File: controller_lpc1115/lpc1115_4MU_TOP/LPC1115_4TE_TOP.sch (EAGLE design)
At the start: 102 parts, among them P2 ISP, Q1 BC856, Q2 BCP52, Q3 BC847C, U1 LPC1115FBD48, U2 BD9G101, U3 XO32 12MHz

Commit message: [ctrl_4MU_TOP] - v2.0 alpha
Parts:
- added C25: 100nF, rcl:C-EUC1206
- C2: value 470n -> 470nF
- C20, C6: device rcl:C-EUC1206 -> rcl:C-EUC0805
- renumbered D9 to D100
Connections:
- net +3V3: now also C25.1
- net GND: now also C25.2
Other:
- moved on the sheet: C7
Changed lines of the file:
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@@
 <part name="L1" library="rcl" library_urn="urn:adsk.eagle:library:334" deviceset="L-EU" device="L4532P" package3d_urn="urn:adsk.eagle:package:23484/1" value="4.7uH"/>
 <part name="C4" library="rcl" library_urn="urn:adsk.eagle:library:334" deviceset="C-EU" device="C0805" package3d_urn="urn:adsk.eagle:package:23617/2" value="4.7uF 50V"/>
-<part name="C6" library="rcl" library_urn="urn:adsk.eagle:library:334" deviceset="C-EU" device="C1206" package3d_urn="urn:adsk.eagle:package:23618/2" value="47uF 10V"/>
+<part name="C6" library="rcl" library_urn="urn:adsk.eagle:library:334" deviceset="C-EU" device="C0805" package3d_urn="urn:adsk.eagle:package:23617/2" value="47uF 10V"/>
 <part name="C1" library="rcl" library_urn="urn:adsk.eagle:library:334" deviceset="C-EU" device="C0805" package3d_urn="urn:adsk.eagle:package:23617/2" value="15nF"/>
 <part name="R2" library="rcl" library_urn="urn:adsk.eagle:library:334" deviceset="R-EU_" device="R0805" package3d_urn="urn:adsk.eagle:package:23553/2" value="1k6"/>
 <part name="R5" library="rcl" library_urn="urn:adsk.eagle:library:334" deviceset="R-EU_" device="R0805" package3d_urn="urn:adsk.eagle:package:23553/2" value="470R"/>
-<part name="C2" library="rcl" library_urn="urn:adsk.eagle:library:334" deviceset="C-EU" device="C0805" package3d_urn="urn:adsk.eagle:package:23617/2" value="470n"/>
-<part name="D9" library="diode" deviceset="DIODE-" device="SOD123" value="RB060M-60(*)"/>
+<part name="C2" library="rcl" library_urn="urn:adsk.eagle:library:334" deviceset="C-EU" device="C0805" package3d_urn="urn:adsk.eagle:package:23617/2" value="470nF"/>
+<part name="D100" library="diode" deviceset="DIODE-" device="SOD123" value="RB060M-60(*)"/>
 <part name="+3V35" library="supply1" deviceset="+3V3" device=""/>
 <part name="C13" library="rcl" library_urn="urn:adsk.eagle:library:334" deviceset="C-EU" device="C0805" package3d_urn="urn:adsk.eagle:package:23617/2" value="1uF"/>
@@
 <part name="D15" library="Diode_for_Selfbus-Projects" deviceset="DIODE-ZENER" device="SOD-123" package3d_urn="urn:adsk.eagle:package:40015434/2" value="DDZ9685"/>
 <part name="R1" library="rcl" library_urn="urn:adsk.eagle:library:334" deviceset="R-EU_" device="R2512" package3d_urn="urn:adsk.eagle:package:23545/2" value="24R  2512 1.0W"/>
-<part name="C20" library="rcl" library_urn="urn:adsk.eagle:library:334" deviceset="C-EU" device="C1206" package3d_urn="urn:adsk.eagle:package:23618/2" value="47uF 10V"/>
+<part name="C20" library="rcl" library_urn="urn:adsk.eagle:library:334" deviceset="C-EU" device="C0805" package3d_urn="urn:adsk.eagle:package:23617/2" value="47uF 10V"/>
 <part name="GND4" library="supply1" deviceset="GND" device=""/>
 <part name="C21" library="rcl" library_urn="urn:adsk.eagle:library:334" deviceset="C-EU" device="C0805" package3d_urn="urn:adsk.eagle:package:23617/2" value="100nF"/>
 <part name="C8" library="rcl" library_urn="urn:adsk.eagle:library:334" deviceset="C-EU" device="C0805" package3d_urn="urn:adsk.eagle:package:23617/2" value="100nF"/>
 <part name="C24" library="rcl" library_urn="urn:adsk.eagle:library:334" deviceset="C-EU" device="C0805" package3d_urn="urn:adsk.eagle:package:23617/2" value="1uF"/>
+<part name="C25" library="rcl" library_urn="urn:adsk.eagle:library:334" deviceset="C-EU" device="C1206" package3d_urn="urn:adsk.eagle:package:23618/2" value="100nF"/>
+<part name="GND7" library="supply1" deviceset="GND" device=""/>
 </parts>
 <sheets>
@@
 <instance part="C6" gate="G$1" x="200.66" y="226.06" smashed="yes">
 <attribute name="NAME" x="202.184" y="226.441" size="1.778" layer="95"/>
-<attribute name="VALUE" x="206.629" y="211.074" size="1.778" layer="96" rot="R90"/>
+<attribute name="VALUE" x="201.549" y="190.754" size="1.778" layer="96" rot="R90"/>
 </instance>
 <instance part="C1" gate="G$1" x="147.32" y="233.68" smashed="yes" rot="R270">
@@
 <attribute name="VALUE" x="181.356" y="226.441" size="1.778" layer="96" rot="MR0"/>
 </instance>
-<instance part="D9" gate="G$1" x="160.02" y="223.52" smashed="yes" rot="R90">
+<instance part="D100" gate="G$1" x="160.02" y="223.52" smashed="yes" rot="R90">
 <attribute name="NAME" x="159.5374" y="226.06" size="1.778" layer="95" rot="R90"/>
 <attribute name="VALUE" x="162.3314" y="226.06" size="1.778" layer="96" rot="R90"/>
@@
 <attribute name="SHEET" x="357.505" y="5.08" size="2.54" layer="94"/>
 </instance>
-<instance part="C7" gate="G$1" x="215.9" y="226.06" smashed="yes">
-<attribute name="NAME" x="217.043" y="226.5426" size="1.778" layer="95"/>
-</instance>
-<instance part="GND10" gate="1" x="215.9" y="208.28" smashed="yes">
-<attribute name="VALUE" x="213.36" y="205.74" size="1.778" layer="96"/>
+<instance part="C7" gate="G$1" x="226.06" y="226.06" smashed="yes">
+<attribute name="NAME" x="227.203" y="226.5426" size="1.778" layer="95"/>
+</instance>
+<instance part="GND10" gate="1" x="226.06" y="208.28" smashed="yes">
+<attribute name="VALUE" x="223.52" y="205.74" size="1.778" layer="96"/>
 </instance>
 <instance part="D16" gate="G$1" x="60.96" y="127" smashed="yes" rot="R90">
@@
 <instance part="C20" gate="G$1" x="208.28" y="226.06" smashed="yes">
 <attribute name="NAME" x="209.804" y="226.441" size="1.778" layer="95"/>
-<attribute name="VALUE" x="214.249" y="211.074" size="1.778" layer="96" rot="R90"/>
+<attribute name="VALUE" x="209.169" y="190.754" size="1.778" layer="96" rot="R90"/>
 </instance>
 <instance part="GND4" gate="1" x="208.28" y="208.28" smashed="yes">
@@
 <attribute name="NAME" x="301.244" y="91.821" size="1.778" layer="95"/>
 <attribute name="VALUE" x="301.244" y="86.741" size="1.778" layer="96"/>
+</instance>
+<instance part="C25" gate="G$1" x="215.9" y="226.06" smashed="yes">
+<attribute name="NAME" x="217.424" y="226.441" size="1.778" layer="95"/>
+<attribute name="VALUE" x="216.789" y="190.754" size="1.778" layer="96" rot="R90"/>
+</instance>
+<instance part="GND7" gate="1" x="215.9" y="208.28" smashed="yes">
+<attribute name="VALUE" x="213.36" y="205.74" size="1.778" layer="96"/>
 </instance>
 </instances>
@@
 </segment>
 <segment>
-<pinref part="D9" gate="G$1" pin="A"/>
+<pinref part="D100" gate="G$1" pin="A"/>
 <wire x1="160.02" y1="220.98" x2="160.02" y2="210.82" width="0.1524" layer="91"/>
 <pinref part="GND6" gate="1" pin="GND"/>
@@
 <pinref part="C7" gate="G$1" pin="-"/>
 <pinref part="GND10" gate="1" pin="GND"/>
-<wire x1="215.9" y1="220.98" x2="215.9" y2="210.82" width="0.1524" layer="91"/>
+<wire x1="226.06" y1="220.98" x2="226.06" y2="210.82" width="0.1524" layer="91"/>
 </segment>
 <segment>
@@
 <wire x1="208.28" y1="220.98" x2="208.28" y2="210.82" width="0.1524" layer="91"/>
 <pinref part="GND4" gate="1" pin="GND"/>
+</segment>
+<segment>
+<pinref part="C25" gate="G$1" pin="2"/>
+<wire x1="215.9" y1="220.98" x2="215.9" y2="210.82" width="0.1524" layer="91"/>
+<pinref part="GND7" gate="1" pin="GND"/>
 </segment>
 </net>
@@
 <wire x1="152.4" y1="233.68" x2="152.4" y2="238.76" width="0.1524" layer="91"/>
 <pinref part="L1" gate="G$1" pin="1"/>
-<pinref part="D9" gate="G$1" pin="C"/>
+<pinref part="D100" gate="G$1" pin="C"/>
 <wire x1="160.02" y1="226.06" x2="160.02" y2="238.76" width="0.1524" layer="91"/>
 <junction x="152.4" y="238.76"/>
@@
 <wire x1="200.66" y1="238.76" x2="208.28" y2="238.76" width="0.1524" layer="91"/>
 <wire x1="208.28" y1="238.76" x2="215.9" y2="238.76" width="0.1524" layer="91"/>
-<wire x1="215.9" y1="238.76" x2="223.52" y2="238.76" width="0.1524" layer="91"/>
+<wire x1="215.9" y1="238.76" x2="226.06" y2="238.76" width="0.1524" layer="91"/>
+<wire x1="226.06" y1="238.76" x2="223.52" y2="238.76" width="0.1524" layer="91"/>
 <wire x1="223.52" y1="238.76" x2="231.14" y2="238.76" width="0.1524" layer="91"/>
 <wire x1="190.5" y1="236.22" x2="190.5" y2="238.76" width="0.1524" layer="91"/>
@@
 <junction x="200.66" y="238.76"/>
 <pinref part="C7" gate="G$1" pin="+"/>
-<wire x1="215.9" y1="238.76" x2="215.9" y2="228.6" width="0.1524" layer="91"/>
-<junction x="215.9" y="238.76"/>
+<wire x1="226.06" y1="238.76" x2="226.06" y2="228.6" width="0.1524" layer="91"/>
+<junction x="226.06" y="238.76"/>
 <pinref part="C20" gate="G$1" pin="1"/>
 <wire x1="208.28" y1="228.6" x2="208.28" y2="238.76" width="0.1524" layer="91"/>
 <junction x="208.28" y="238.76"/>
-</segment>
-<segment>
+<pinref part="C25" gate="G$1" pin="1"/>
+<wire x1="215.9" y1="228.6" x2="215.9" y2="238.76" width="0.1524" layer="91"/>
+<junction x="215.9" y="238.76"/>
+</segment>
+<segment>

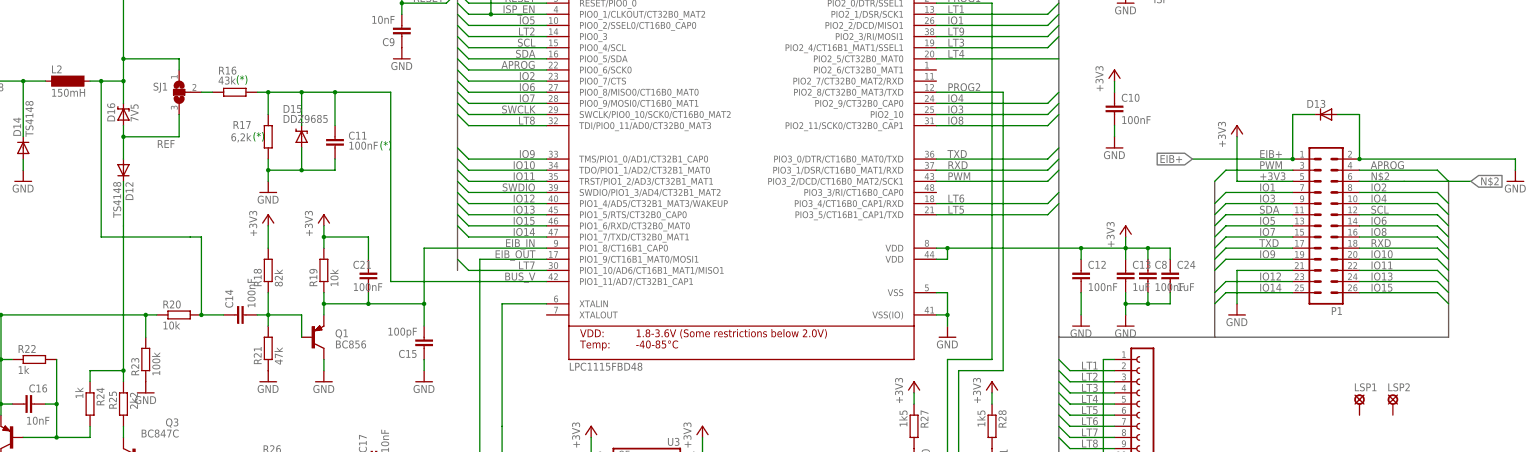
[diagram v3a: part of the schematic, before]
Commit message: [ctrl_4MU_TOP] - intermediate status of re-routing
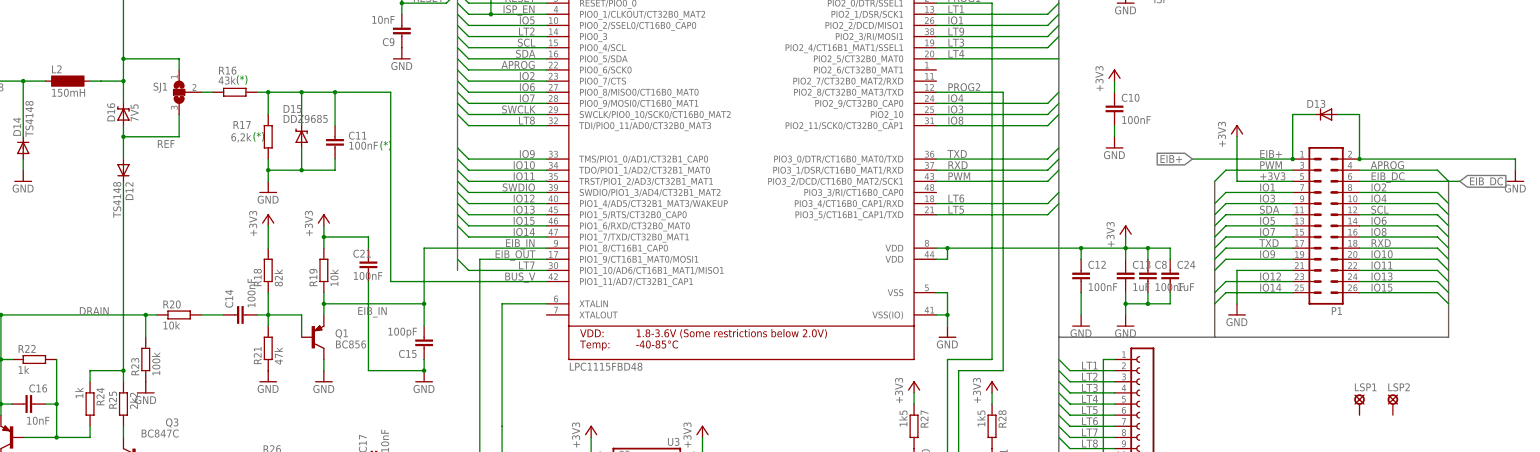
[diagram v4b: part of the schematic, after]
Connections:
- removed net N$2: P1.6
- new net N$3: C14.1, R20.2
- net EIB_DC: now also P1.6; no longer C14.1, R20.2
- net EIB_IN: no longer C21.1
- net GND: now also C21.1
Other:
- moved on the sheet: C21
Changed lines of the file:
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@@
 <attribute name="VALUE" x="205.74" y="205.74" size="1.778" layer="96"/>
 </instance>
-<instance part="C21" gate="G$1" x="116.84" y="88.9" smashed="yes" rot="R180">
-<attribute name="NAME" x="113.284" y="91.821" size="1.778" layer="95"/>
-<attribute name="VALUE" x="113.284" y="86.741" size="1.778" layer="96"/>
+<instance part="C21" gate="G$1" x="116.84" y="91.44" smashed="yes" rot="R180">
+<attribute name="NAME" x="113.284" y="94.361" size="1.778" layer="95"/>
+<attribute name="VALUE" x="113.284" y="89.281" size="1.778" layer="96"/>
 </instance>
 <instance part="C8" gate="G$1" x="294.64" y="91.44" smashed="yes">
@@
 <pinref part="C15" gate="G$1" pin="1"/>
 <wire x1="129.54" y1="68.58" x2="129.54" y2="71.12" width="0.1524" layer="91"/>
+<pinref part="C21" gate="G$1" pin="1"/>
+<wire x1="116.84" y1="88.9" x2="116.84" y2="68.58" width="0.1524" layer="91"/>
+<wire x1="116.84" y1="68.58" x2="129.54" y2="68.58" width="0.1524" layer="91"/>
+<junction x="129.54" y="68.58"/>
 </segment>
 <segment>
@@
 <wire x1="129.54" y1="83.82" x2="116.84" y2="83.82" width="0.1524" layer="91"/>
 <junction x="106.68" y="83.82"/>
-<pinref part="C21" gate="G$1" pin="1"/>
 <wire x1="116.84" y1="83.82" x2="106.68" y2="83.82" width="0.1524" layer="91"/>
-<wire x1="116.84" y1="86.36" x2="116.84" y2="83.82" width="0.1524" layer="91"/>
-<junction x="116.84" y="83.82"/>
+<label x="114.3" y="81.28" size="1.778" layer="95"/>
 </segment>
 </net>
@@
 <wire x1="60.96" y1="129.54" x2="60.96" y2="134.62" width="0.1524" layer="91"/>
 <junction x="60.96" y="134.62"/>
-<pinref part="C14" gate="G$1" pin="1"/>
-<pinref part="R20" gate="G$1" pin="2"/>
-<wire x1="83.82" y1="81.28" x2="78.74" y2="81.28" width="0.1524" layer="91"/>
-<wire x1="78.74" y1="81.28" x2="78.74" y2="99.06" width="0.1524" layer="91"/>
-<wire x1="78.74" y1="99.06" x2="76.2" y2="99.06" width="0.1524" layer="91"/>
-<junction x="78.74" y="81.28"/>
-<wire x1="76.2" y1="99.06" x2="55.88" y2="99.06" width="0.1524" layer="91"/>
-<wire x1="55.88" y1="99.06" x2="55.88" y2="134.62" width="0.1524" layer="91"/>
-<junction x="55.88" y="134.62"/>
+</segment>
+<segment>
+<pinref part="P1" gate="1" pin="6"/>
+<wire x1="342.9" y1="111.76" x2="350.52" y2="111.76" width="0.1524" layer="91"/>
+<wire x1="350.52" y1="111.76" x2="365.76" y2="111.76" width="0.1524" layer="91"/>
+<label x="345.44" y="112.014" size="1.778" layer="95"/>
+<label x="365.76" y="111.76" size="1.778" layer="95" xref="yes"/>
 </segment>
 </net>
@@
 <wire x1="68.58" y1="81.28" x2="66.04" y2="81.28" width="0.1524" layer="91"/>
 <junction x="66.04" y="81.28"/>
+<label x="50.8" y="81.28" size="1.778" layer="95"/>
 </segment>
 </net>
@@
 <pinref part="C21" gate="G$1" pin="2"/>
 <wire x1="106.68" y1="99.06" x2="106.68" y2="101.6" width="0.1524" layer="91"/>
-<wire x1="116.84" y1="93.98" x2="116.84" y2="99.06" width="0.1524" layer="91"/>
+<wire x1="116.84" y1="96.52" x2="116.84" y2="99.06" width="0.1524" layer="91"/>
 <wire x1="116.84" y1="99.06" x2="106.68" y2="99.06" width="0.1524" layer="91"/>
 <junction x="106.68" y="99.06"/>
@@
 </segment>
 </net>
-<net name="N$2" class="0">
-<segment>
-<pinref part="P1" gate="1" pin="6"/>
-<wire x1="342.9" y1="111.76" x2="353.06" y2="111.76" width="0.1524" layer="91"/>
-<wire x1="353.06" y1="111.76" x2="368.3" y2="111.76" width="0.1524" layer="91"/>
-<label x="345.44" y="112.014" size="1.778" layer="95"/>
-<label x="368.3" y="111.76" size="1.778" layer="95" xref="yes"/>
-</segment>
-</net>
+<net name="N$3" class="0">
+<segment>
+<pinref part="R20" gate="G$1" pin="2"/>
+<pinref part="C14" gate="G$1" pin="1"/>
+<wire x1="83.82" y1="81.28" x2="78.74" y2="81.28" width="0.1524" layer="91"/>
+</segment>
+</net>
